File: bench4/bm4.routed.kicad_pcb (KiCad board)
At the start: 2 copper layers, 40 x 41 mm, 48 parts

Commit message: has changed obstacles logic v1
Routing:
- net /SPOLN: track 0.00 -> 15.9 mm, vias 0 -> 2
- net GND: track 123.7 -> 122.0 mm, vias 16 -> 0
- net /SPKVDD: track 20.7 -> 21.3 mm, vias 4 -> 2

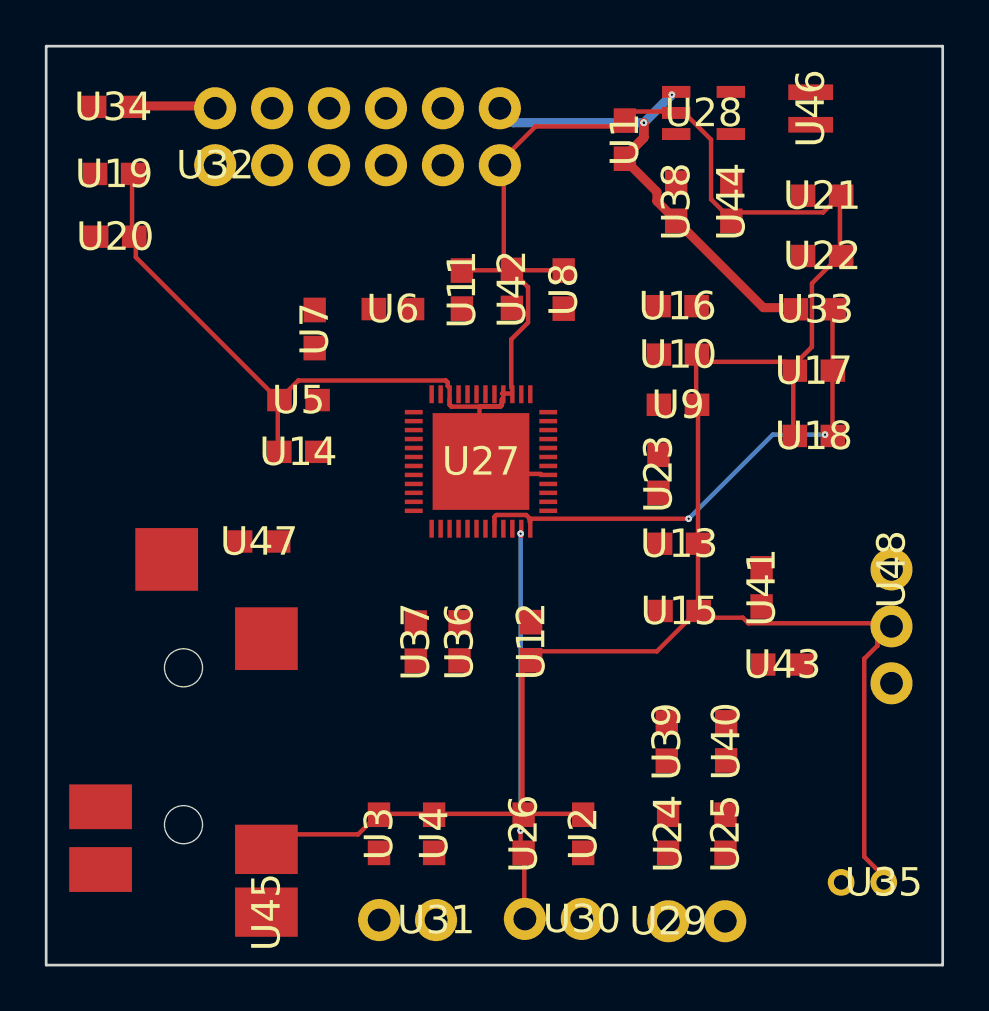
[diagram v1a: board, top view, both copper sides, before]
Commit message: prepare to add pad shape
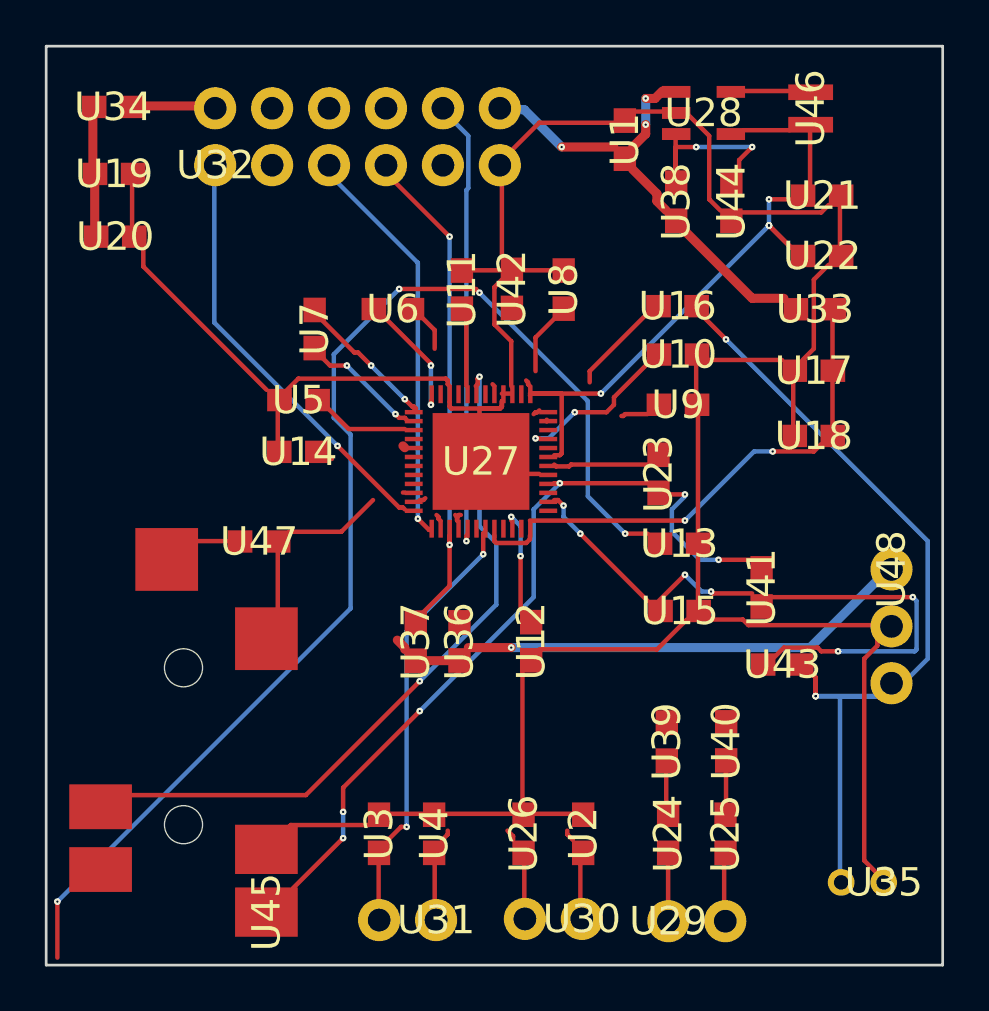
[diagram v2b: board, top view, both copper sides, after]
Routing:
- net Net-(C21-Pad2): track 0.00 -> 54.9 mm, vias 0 -> 4
- net /IN2P: track 0.00 -> 39.7 mm, vias 0 -> 3
- net /IN1P: track 0.00 -> 34.3 mm, vias 0 -> 6
- net /HPOR: track 0.00 -> 30.8 mm, vias 0 -> 2
- net /1.8VDD: track 0.00 -> 28.2 mm, vias 0 -> 4
- net /MICBIAS1: track 0.00 -> 26.8 mm, vias 0 -> 6
- net /3.3VDD: track 0.00 -> 25.5 mm, vias 0 -> 1
- net /XADUIO_SCL: track 0.00 -> 21.8 mm, vias 0 -> 2
- net /XAUDIO_IRQ: track 0.00 -> 19.3 mm, vias 0 -> 1
- net /XADUIO_I2S0_LRCKL: track 0.00 -> 18.5 mm, vias 0 -> 1
- net /XADUIO_I2S0_BCLK: track 0.00 -> 17.6 mm, vias 0 -> 1
- net /SPORN: track 0.00 -> 17.6 mm, vias 0 -> 2
- net /SPOLN: track 15.9 -> 2.44 mm, vias 2 -> 0
- net Net-(IC2-Pad3): track 0.00 -> 7.36 mm, vias 0 -> 2
- net /HPOL: track 0.00 -> 7.25 mm
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
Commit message: optimized via cost
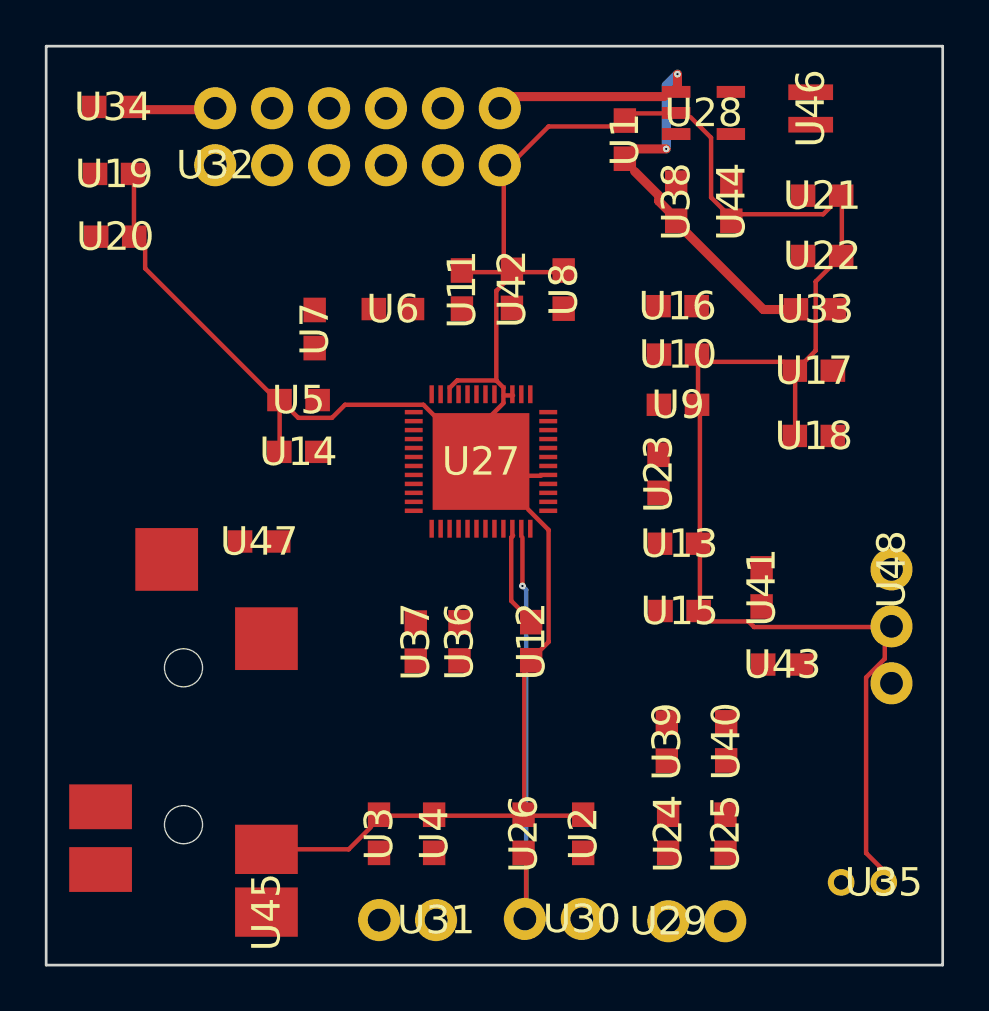
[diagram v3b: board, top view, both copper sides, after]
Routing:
- net Net-(C21-Pad2): track 54.9 -> 0.00 mm, vias 4 -> 0
- net /IN2P: track 39.7 -> 0.00 mm, vias 3 -> 0
- net /IN1P: track 34.3 -> 0.00 mm, vias 6 -> 0
- net /HPOR: track 30.8 -> 0.00 mm, vias 2 -> 0
- net /1.8VDD: track 28.2 -> 0.00 mm, vias 4 -> 0
- net /MICBIAS1: track 26.8 -> 0.00 mm, vias 6 -> 0
- net /3.3VDD: track 25.5 -> 0.00 mm, vias 1 -> 0
- net /XADUIO_SCL: track 21.8 -> 0.00 mm, vias 2 -> 0
- net /XAUDIO_IRQ: track 19.3 -> 0.00 mm, vias 1 -> 0
- net /XADUIO_I2S0_LRCKL: track 18.5 -> 0.00 mm, vias 1 -> 0
- net /XADUIO_I2S0_BCLK: track 17.6 -> 0.00 mm, vias 1 -> 0
- net /SPORN: track 17.6 -> 0.00 mm, vias 2 -> 0
- net Net-(IC2-Pad3): track 7.36 -> 0.00 mm, vias 2 -> 0
- net /HPOL: track 7.25 -> 0.00 mm
- net Net-(C19-Pad2): track 6.74 -> 0.00 mm, vias 2 -> 0
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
